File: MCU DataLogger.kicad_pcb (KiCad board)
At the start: 4 copper layers, 51 x 35 mm, 29 parts, among them J1 Conn_01x04_Pin, J2 Conn_01x09_Pin, J3 Conn_01x04_Pin, J4 Conn_02x03_Odd_Even, U1 24LC1025, U2 DS1337S_, U3 24LC1025, U4 ATMEGA328P-AU, Y1 32.768 KH, Y2 16MHz

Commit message: Staging for schematic bug fixes
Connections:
- net Net-(U4-AREF) renamed /ABC123
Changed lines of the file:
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@@
 			(layers "F.Cu" "F.Mask" "F.Paste")
 			(roundrect_rratio 0.125)
-			(net "Net-(U4-AREF)")
+			(net "/ABC123")
 			(pinfunction "AREF_20")
 			(pintype "input")
@@
 			(layers "F.Cu" "F.Mask" "F.Paste")
 			(roundrect_rratio 0.25)
-			(net "Net-(U4-AREF)")
+			(net "/ABC123")
 			(pintype "passive")
 		)
@@
 	)
 	(segment
-		(start 128.09 74.15)
-		(end 128.825 74.15)
-		(width 0.2)
-		(layer "F.Cu")
-		(net "Net-(U4-AREF)")
-	)
-	(segment
-		(start 131.0132 84.1248)
-		(end 131.0132 86.250214)
-		(width 0.2)
-		(layer "F.Cu")
-		(net "Net-(U4-AREF)")
-	)
-	(segment
-		(start 131.0132 86.250214)
-		(end 132.211093 87.448107)
-		(width 0.2)
-		(layer "F.Cu")
-		(net "Net-(U4-AREF)")
-	)
-	(segment
-		(start 133.0925 85.9571)
-		(end 133.0925 84)
-		(width 0.2)
-		(layer "F.Cu")
-		(net "Net-(U4-AREF)")
-	)
-	(segment
-		(start 133.0452 86.0044)
-		(end 133.0925 85.9571)
-		(width 0.2)
-		(layer "F.Cu")
-		(net "Net-(U4-AREF)")
-	)
-	(segment
-		(start 128.825 74.15)
-		(end 131.1496 76.4746)
-		(width 0.2)
-		(layer "F.Cu")
-		(net "Net-(U4-AREF)")
-	)
-	(segment
-		(start 131.1496 76.4746)
-		(end 131.1496 83.9884)
-		(width 0.2)
-		(layer "F.Cu")
-		(net "Net-(U4-AREF)")
-	)
-	(segment
-		(start 131.1496 83.9884)
-		(end 131.0132 84.1248)
-		(width 0.2)
-		(layer "F.Cu")
-		(net "Net-(U4-AREF)")
-	)
-	(via
-		(at 132.211093 87.448107)
-		(size 0.6)
-		(drill 0.3)
-		(layers "F.Cu" "B.Cu")
-		(net "Net-(U4-AREF)")
-	)
-	(via
-		(at 133.0452 86.0044)
-		(size 0.6)
-		(drill 0.3)
-		(layers "F.Cu" "B.Cu")
-		(net "Net-(U4-AREF)")
-	)
-	(segment
-		(start 132.211093 87.448107)
-		(end 132.211093 86.838507)
-		(width 0.2)
-		(layer "B.Cu")
-		(net "Net-(U4-AREF)")
-	)
-	(segment
-		(start 132.211093 86.838507)
-		(end 133.0452 86.0044)
-		(width 0.2)
-		(layer "B.Cu")
-		(net "Net-(U4-AREF)")
-	)
-	(segment
 		(start 141.5572 75.3872)
 		(end 133.1468 75.3872)
@@
 		(net "Net-(U2-X2)")
 	)
+	(segment
+		(start 128.09 74.15)
+		(end 128.825 74.15)
+		(width 0.2)
+		(layer "F.Cu")
+		(net "/ABC123")
+	)
+	(segment
+		(start 131.0132 84.1248)
+		(end 131.0132 86.250214)
+		(width 0.2)
+		(layer "F.Cu")
+		(net "/ABC123")
+	)
+	(segment
+		(start 131.0132 86.250214)
+		(end 132.211093 87.448107)
+		(width 0.2)
+		(layer "F.Cu")
+		(net "/ABC123")
+	)
+	(segment
+		(start 133.0925 85.9571)
+		(end 133.0925 84)
+		(width 0.2)
+		(layer "F.Cu")
+		(net "/ABC123")
+	)
+	(segment
+		(start 133.0452 86.0044)
+		(end 133.0925 85.9571)
+		(width 0.2)
+		(layer "F.Cu")
+		(net "/ABC123")
+	)
+	(segment
+		(start 128.825 74.15)
+		(end 131.1496 76.4746)
+		(width 0.2)
+		(layer "F.Cu")
+		(net "/ABC123")
+	)
+	(segment
+		(start 131.1496 76.4746)
+		(end 131.1496 83.9884)
+		(width 0.2)
+		(layer "F.Cu")
+		(net "/ABC123")
+	)
+	(segment
+		(start 131.1496 83.9884)
+		(end 131.0132 84.1248)
+		(width 0.2)
+		(layer "F.Cu")
+		(net "/ABC123")
+	)
+	(via
+		(at 132.211093 87.448107)
+		(size 0.6)
+		(drill 0.3)
+		(layers "F.Cu" "B.Cu")
+		(net "/ABC123")
+	)
+	(via
+		(at 133.0452 86.0044)
+		(size 0.6)
+		(drill 0.3)
+		(layers "F.Cu" "B.Cu")
+		(net "/ABC123")
+	)
+	(segment
+		(start 132.211093 87.448107)
+		(end 132.211093 86.838507)
+		(width 0.2)
+		(layer "B.Cu")
+		(net "/ABC123")
+	)
+	(segment
+		(start 132.211093 86.838507)
+		(end 133.0452 86.0044)
+		(width 0.2)
+		(layer "B.Cu")
+		(net "/ABC123")
+	)
 	(zone

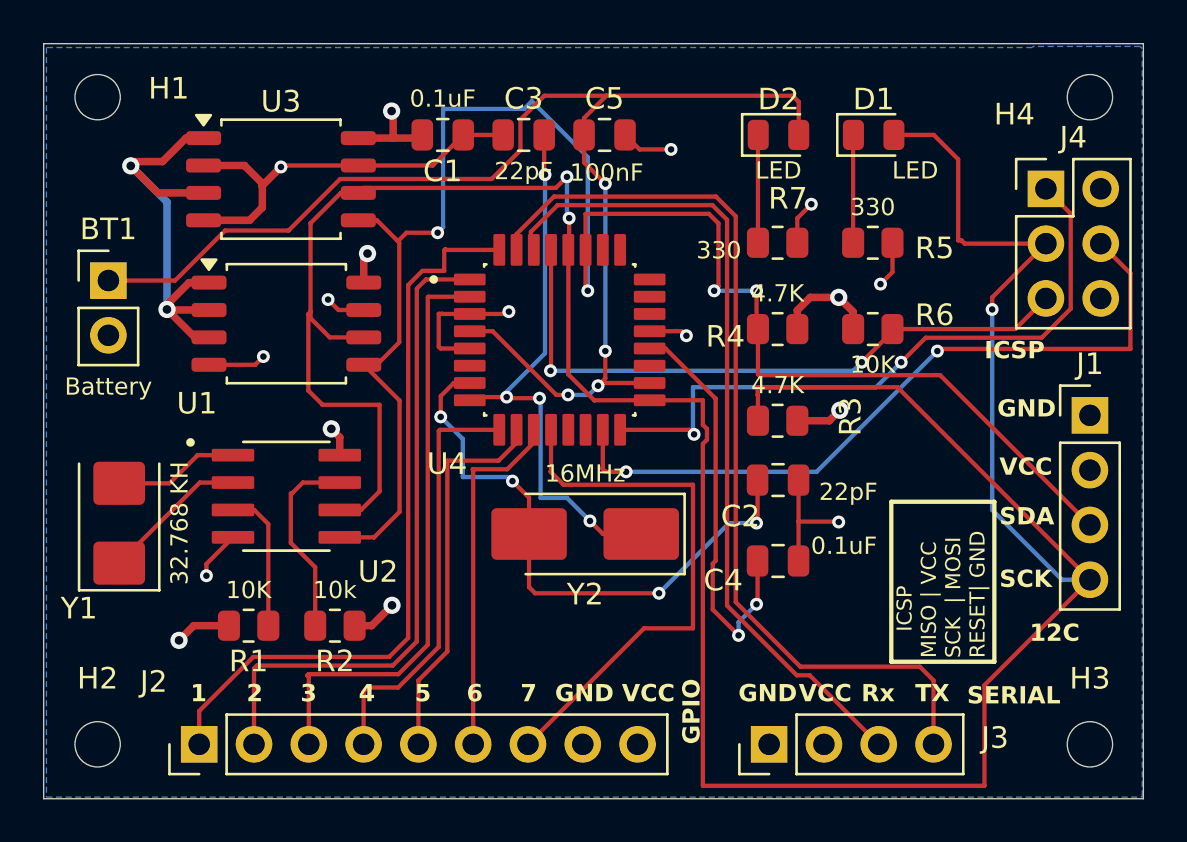
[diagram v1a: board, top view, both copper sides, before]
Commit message: Fixed the SCL vs SCK net list errors routing in the 4layer
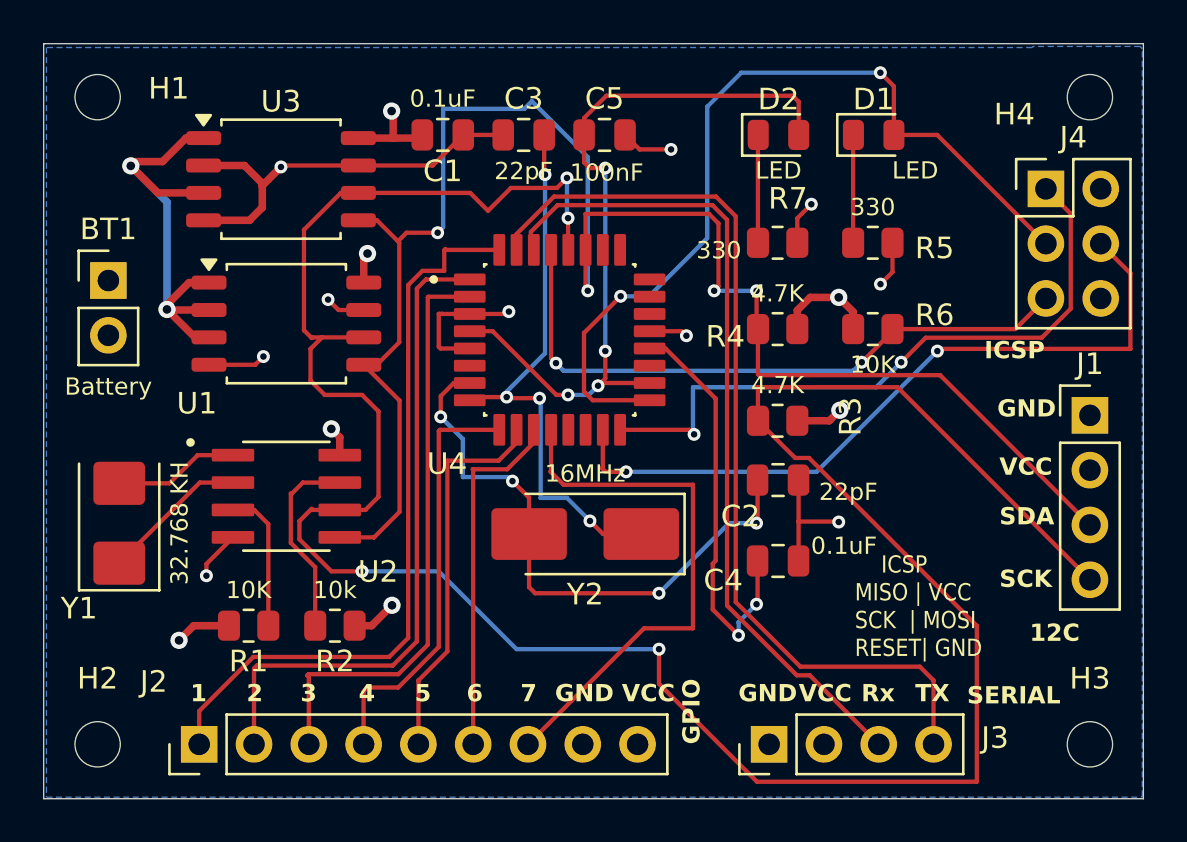
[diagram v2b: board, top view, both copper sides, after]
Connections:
- BT1 pad 1: Net-(BT1-+) -> /Vcc
- C5 pad 1: Net-(BT1-+) -> /Vcc
- D2 pad 2: Net-(BT1-+) -> /Vcc
- J1 pad 4: /SCK -> /SCL
- R3 pad 2: /SCK -> /SCL
- U1 pad 6: /SCK -> /SCL
- U2 pad 6: /SCK -> /SCL
- U3 pad 6: /SCK -> /SCL
- U4 pad 18: Net-(BT1-+) -> /Vcc
- U4 pad 28: /SCK -> /SCL
- U4 pad 4: Net-(BT1-+) -> /Vcc
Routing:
- net /SCL: track 0.00 -> 118.7 mm, vias 0 -> 4
- net /SCK: track 143.4 -> 40.5 mm, vias 3 -> 2
- net Net-(BT1-+): track 62.2 -> 0.00 mm, vias 4 -> 0
- net /Vcc: track 41.0 -> 76.2 mm, vias 9 -> 13
